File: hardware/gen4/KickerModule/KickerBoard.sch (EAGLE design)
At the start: 111 parts

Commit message: motor board almost done
motor board almost done and also mainboard
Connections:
- net BB_IN: now also COM_BOARD.7
- net BB_OUT: now also COM_BOARD.9
- net CHIP_ENABLE: now also COM_BOARD.13
- net DISCHARGE: now also COM_BOARD.16, COM_BOARD.18
- net DIVCAP: now also COM_BOARD.14
- net KICK_ENABLE: now also COM_BOARD.11
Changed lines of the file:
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@@
 <pinref part="R8" gate="G$1" pin="2"/>
 <wire x1="337.82" y1="266.7" x2="337.82" y2="274.32" width="0.1524" layer="91"/>
-<wire x1="337.82" y1="266.7" x2="347.98" y2="266.7" width="0.1524" layer="91"/>
+<wire x1="337.82" y1="266.7" x2="342.9" y2="266.7" width="0.1524" layer="91"/>
 <label x="337.82" y="271.78" size="1.778" layer="95"/>
+<label x="543.56" y="154.94" size="1.778" layer="95"/>
+</segment>
+<segment>
+<pinref part="COM_BOARD" gate="G$1" pin="14"/>
+<wire x1="541.02" y1="154.94" x2="551.18" y2="154.94" width="0.1524" layer="91"/>
 </segment>
 </net>
@@
 <wire x1="294.64" y1="281.94" x2="294.64" y2="279.4" width="0.1524" layer="91"/>
 <junction x="294.64" y="281.94"/>
+<label x="264.16" y="281.94" size="1.778" layer="95"/>
+<label x="505.46" y="154.94" size="1.778" layer="95"/>
 </segment>
 <segment>
 <wire x1="330.2" y1="220.98" x2="312.42" y2="223.52" width="0.1524" layer="91"/>
 <label x="312.42" y="223.52" size="1.778" layer="95"/>
+</segment>
+<segment>
+<pinref part="COM_BOARD" gate="G$1" pin="13"/>
+<wire x1="525.78" y1="154.94" x2="510.54" y2="154.94" width="0.1524" layer="91"/>
 </segment>
 </net>
@@
 <wire x1="287.02" y1="284.48" x2="287.02" y2="279.4" width="0.1524" layer="91"/>
 <junction x="287.02" y="284.48"/>
+<label x="505.46" y="157.48" size="1.778" layer="95"/>
 </segment>
 <segment>
 <wire x1="330.2" y1="223.52" x2="312.42" y2="226.06" width="0.1524" layer="91"/>
 <label x="312.42" y="226.06" size="1.778" layer="95"/>
+</segment>
+<segment>
+<pinref part="COM_BOARD" gate="G$1" pin="11"/>
+<wire x1="525.78" y1="157.48" x2="510.54" y2="157.48" width="0.1524" layer="91"/>
 </segment>
 </net>
@@
 <wire x1="584.2" y1="314.96" x2="589.28" y2="314.96" width="0.1524" layer="91"/>
 <label x="586.74" y="314.96" size="1.778" layer="95"/>
+<label x="543.56" y="152.4" size="1.778" layer="95"/>
+</segment>
+<segment>
+<pinref part="COM_BOARD" gate="G$1" pin="18"/>
+<wire x1="541.02" y1="149.86" x2="551.18" y2="149.86" width="0.1524" layer="91"/>
+<junction x="541.02" y="149.86"/>
+</segment>
+<segment>
+<pinref part="COM_BOARD" gate="G$1" pin="16"/>
+<wire x1="541.02" y1="152.4" x2="551.18" y2="152.4" width="0.1524" layer="91"/>
+<junction x="541.02" y="152.4"/>
 </segment>
 </net>
@@
 <wire x1="289.56" y1="350.52" x2="271.78" y2="350.52" width="0.1524" layer="91"/>
 <junction x="289.56" y="350.52"/>
+<label x="543.56" y="149.86" size="1.778" layer="95"/>
 </segment>
 </net>
@@
 <pinref part="R19" gate="G$1" pin="1"/>
 <label x="574.04" y="259.08" size="1.778" layer="95"/>
+<label x="508" y="160.02" size="1.778" layer="95"/>
+</segment>
+<segment>
+<pinref part="COM_BOARD" gate="G$1" pin="9"/>
+<wire x1="525.78" y1="160.02" x2="510.54" y2="160.02" width="0.1524" layer="91"/>
 </segment>
 </net>
@@
 <label x="574.04" y="292.1" size="1.778" layer="95"/>
 <pinref part="BB_CON" gate="G$1" pin="P$2"/>
-</segment>
-</net>
+<label x="508" y="162.56" size="1.778" layer="95"/>
+</segment>
+<segment>
+<pinref part="COM_BOARD" gate="G$1" pin="7"/>
+<wire x1="525.78" y1="162.56" x2="510.54" y2="162.56" width="0.1524" layer="91"/>
+</segment>
+</net>

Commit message: added new discharge circuit - spruced up for design review
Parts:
- removed DISCHARGE_Q, DISCHARGE_Q1: (no value), gen3:N-MOSFETDPAK
- removed DIS_BIAS: 3v, SparkFun-DiscreteSemi:DIODESMA-KIT
- removed MAN-DIS: SWITCH-MOMENTARY-2SMD-4, SparkFun-Electromechanical:SWITCH-MOMENTARY-2SMD-4
- removed R16: 500k, SparkFun-Passives:RESISTOR0805-RES
- removed R35: 10k, SparkFun-Passives:RESISTOR0805-RES
- removed SPARE_HEADER, SPARE_HEADER1: M10SILK_FEMALE_PTH, SparkFun-Connectors:M10SILK_FEMALE_PTH
- added OK1: CNF17GF, optocoupler:CNF17GF
- added R3: 240, SparkFun-Passives:RESISTOR0805-RES
- added U$2: BSP129-NMOS_DEPLETION, kickerchips:BSP129-NMOS_DEPLETION
- R13: value 2k,5w -> 2.5k,30W
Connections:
- removed net N$22: DISCHARGE_Q.G, MAN-DIS.2, R35.2
- new net N$16: R13.1, U$2.DRAIN
- net 12VGND: now also OK1.EMIT, R3.1; no longer DISCHARGE_Q.S, DISCHARGE_Q1.S, DIS_BIAS.A, R35.1
- net CAP+: no longer R16.2
- net CHARGE: now also COM_BOARD.19
- net CHARGE_DONE: now also COM_BOARD.17
- net DISCHARGE: now also OK1.A; no longer DISCHARGE_Q1.G
- net GND: now also OK1.C
- net KICK_REF: now also COM_BOARD.15
- net N$18: now also R3.2, U$2.GATE; no longer DISCHARGE_Q.D, DISCHARGE_Q1.D, R13.1
- net N$21: now also OK1.COL, U$2.SOURCE; no longer DIS_BIAS.C, MAN-DIS.1, R16.1
- net N$27: now also MOTOR1.3
- net N$28: now also COM_BOARD.1, COM_BOARD.3, COM_BOARD.5
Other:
- note added: "BSP129"
- note added: "Discharge Circuitry"
- note added: "depletion mode nmos for auto discharge"
- note added: "solenoid"
- note removed: "Connected to DAC, not sure what the line is named yet"
- note removed: "I dont think we need this"
- note removed: "bias gate for manual discharge"
- note removed: "buffer"
- note removed: "discharge circuitry"
- moved on the sheet: COM_BOARD, FUSE_MOTOR_3, KICKER, MOTOR1, R13

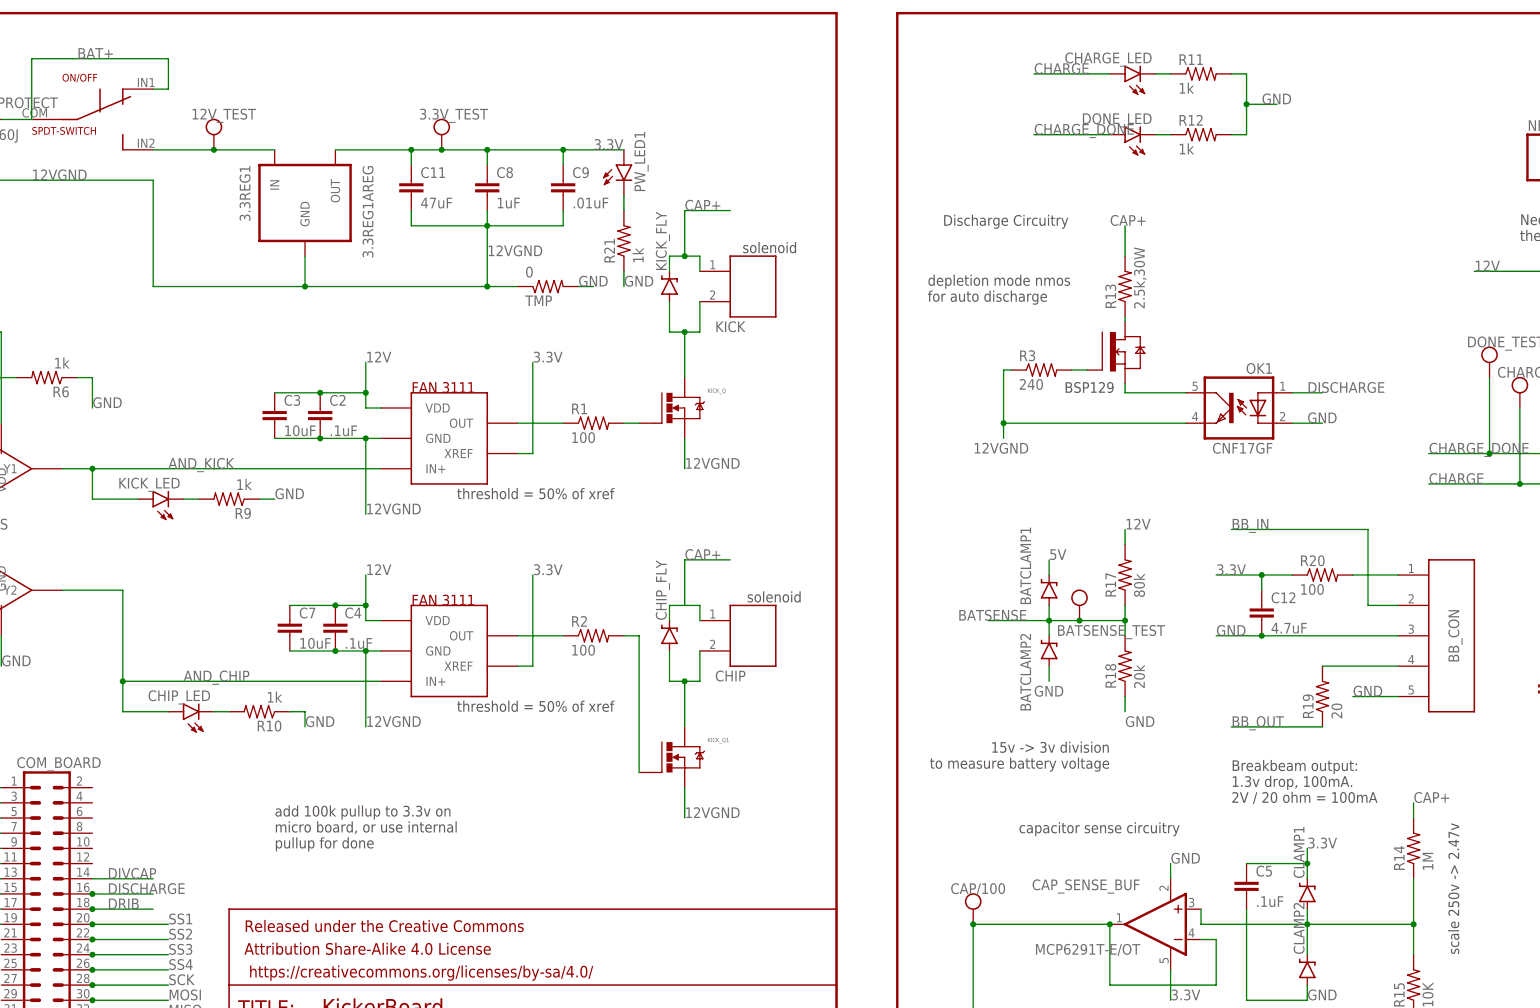
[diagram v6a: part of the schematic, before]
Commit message: added discharge circuit to mainboard + power zener
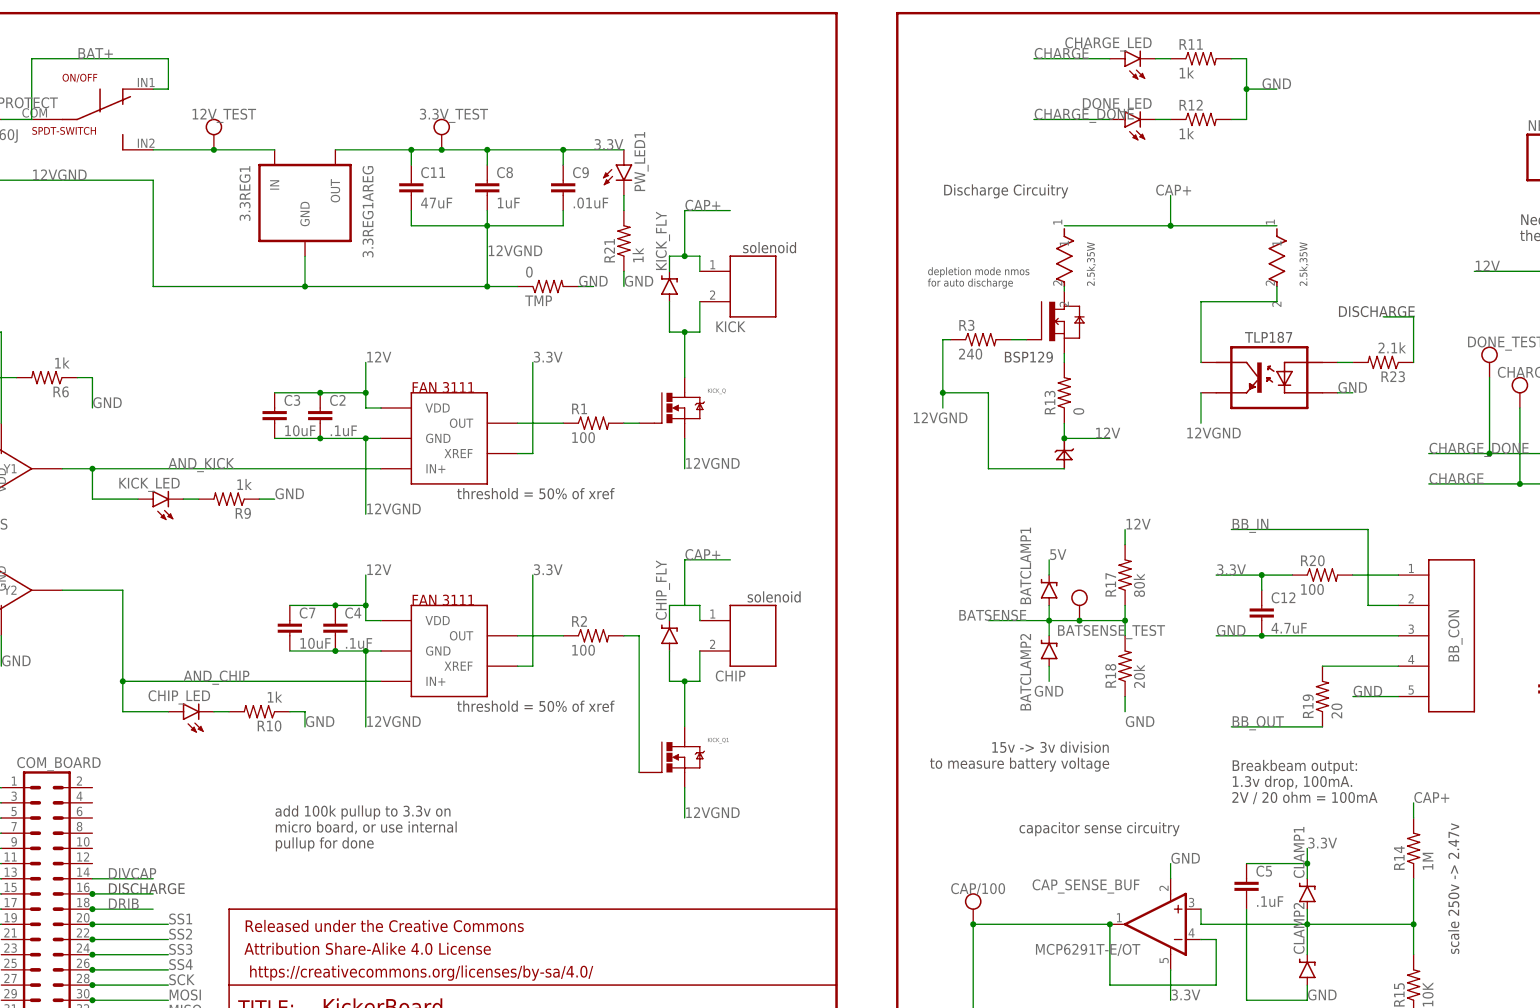
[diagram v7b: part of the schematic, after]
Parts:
- removed OK1: CNF17GF, optocoupler:CNF17GF
- added R16, R22: POWRESISTOR, rfc:POWRESISTOR
- added R23: 2.1k, SparkFun-Passives:RESISTOR0805-RES
- added U$5: TLP187, rfc:TLP187
- added U$6: 13VZENER, rfc:13VZENER
- R13: value 2.5k,30W -> 0; device gen3:RESISTOR -> SparkFun-Passives:RESISTOR0805-RES
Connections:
- new net N$29: R22.2, U$5.DRAIN
- new net N$30: R23.2, U$5.DIODE+
- net 12V: now also R13.1, U$6.-
- net 12VGND: now also U$5.SOURCE, U$6.+; no longer OK1.EMIT
- net CAP+: now also R16.1, R22.1; no longer R13.2
- net DISCHARGE: now also R23.1; no longer OK1.A
- net GND: now also U$5.DIODE-; no longer OK1.C
- net N$16: now also R16.2; no longer R13.1
- net N$21: now also R13.2; no longer OK1.COL
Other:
- note added: "2.5k,35W"
- note added: "DISCHARGE"
- note added: "TLP187"
- moved on the sheet: CHARGE_LED, DONE_LED, R11, R12, R13, R3

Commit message: more preliminary placement
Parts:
- removed C16: 1000uF, rcl:CPOL-USE10-35
- removed FRAME3: FRAME-LETTER, SparkFun-Aesthetics:FRAME-LETTER
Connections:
- net 12VGND: no longer C16.-
- net CAP+: no longer C16.+
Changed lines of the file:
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@@
 <part name="CHIP_FLY" library="gen3" deviceset="DIODE-ZENER" device="DO214AB"/>
 <part name="CHIP" library="gen3" deviceset="JST-2" device="2MM"/>
-<part name="FRAME3" library="SparkFun-Aesthetics" deviceset="FRAME-LETTER" device=""/>
 <part name="R31" library="SparkFun-Passives" deviceset="RESISTOR" device="0805-RES" value="43k"/>
 <part name="RVOUT" library="SparkFun-Passives" deviceset="RESISTOR" device="0805-RES" value="50.4k"/>
@@
 <part name="R24" library="SparkFun-Passives" deviceset="RESISTOR" device="0805-RES" value="536k"/>
 <part name="CAP+_TEST" library="gen3" deviceset="TEST_PT" device=""/>
-<part name="C16" library="rcl" deviceset="CPOL-US" device="E10-35" value="1000uF"/>
 <part name="U$4" library="kickerchips" deviceset="FAN3111" device="1"/>
 <part name="R1" library="SparkFun-Resistors" deviceset="RESISTOR" device="0805-RES" value="100"/>
@@
 <instance part="CHIP_FLY" gate="G$1" x="480.06" y="274.32" rot="R90"/>
 <instance part="CHIP" gate="G$1" x="490.22" y="274.32"/>
-<instance part="FRAME3" gate="G$1" x="518.16" y="193.04"/>
-<instance part="FRAME3" gate="V" x="665.48" y="193.04"/>
 <instance part="R31" gate="G$1" x="675.64" y="299.72"/>
 <instance part="RVOUT" gate="G$1" x="675.64" y="314.96"/>
@@
 <instance part="R24" gate="G$1" x="637.54" y="363.22" rot="R90"/>
 <instance part="CAP+_TEST" gate="G$1" x="678.18" y="370.84"/>
-<instance part="C16" gate="G$1" x="690.88" y="358.14"/>
 <instance part="U$4" gate="G$1" x="444.5" y="307.34"/>
 <instance part="R1" gate="G$1" x="467.36" y="309.88"/>
@@
 <wire x1="678.18" y1="350.52" x2="678.18" y2="345.44" width="0.1524" layer="91"/>
 <label x="678.18" y="345.44" size="1.778" layer="95"/>
-<pinref part="C16" gate="G$1" pin="-"/>
-<wire x1="678.18" y1="350.52" x2="690.88" y2="350.52" width="0.1524" layer="91"/>
-<wire x1="690.88" y1="350.52" x2="690.88" y2="353.06" width="0.1524" layer="91"/>
 <junction x="678.18" y="350.52"/>
 </segment>
@@
 <label x="678.18" y="365.76" size="1.778" layer="95"/>
 <pinref part="CAP+_TEST" gate="G$1" pin="P$1"/>
-<pinref part="C16" gate="G$1" pin="+"/>
-<wire x1="678.18" y1="363.22" x2="690.88" y2="363.22" width="0.1524" layer="91"/>
-<wire x1="690.88" y1="363.22" x2="690.88" y2="360.68" width="0.1524" layer="91"/>
 <junction x="678.18" y="363.22"/>
 </segment>
